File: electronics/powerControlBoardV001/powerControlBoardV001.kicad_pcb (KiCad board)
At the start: 2 copper layers, 100 x 100 mm, 45 parts, among them J1 Conn_01x03, J2 Conn_01x02, J3 Conn_01x02, K1 FINDER-40.52, Q1 Q_NMOS_GSD

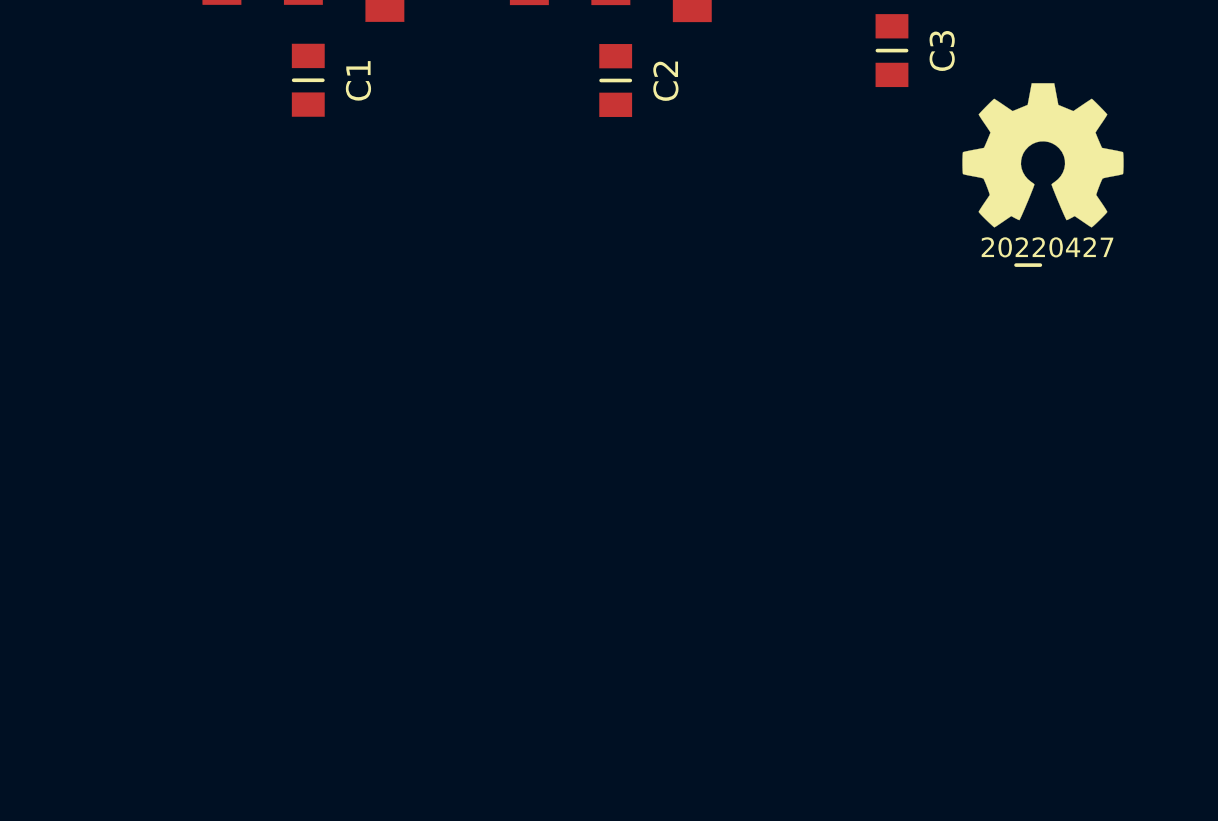
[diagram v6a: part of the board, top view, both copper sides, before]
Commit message: added full zerocross detector
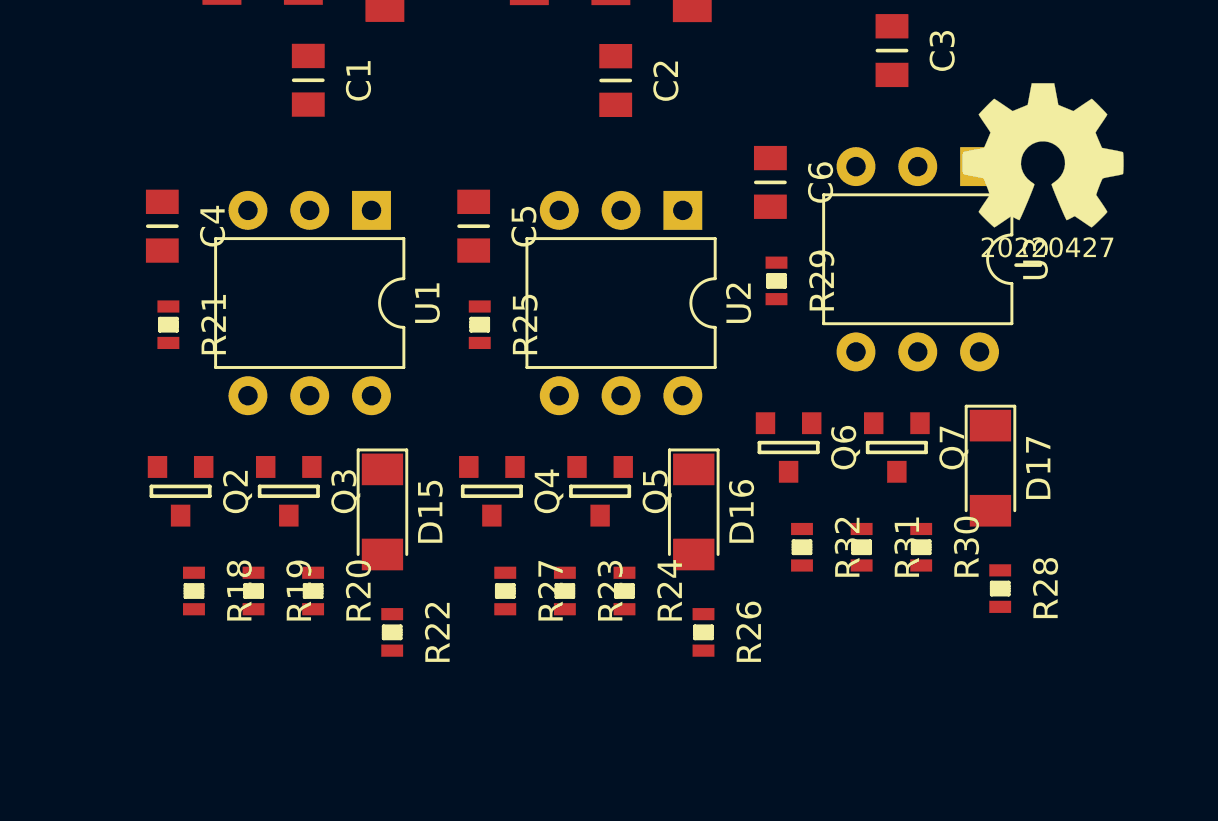
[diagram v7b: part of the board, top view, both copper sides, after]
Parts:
- added C4: 10u, SquantorRcl:C_0805, F.Cu at (102.5, 90.5)
- added C5: 10u, SquantorRcl:C_0805, F.Cu at (115.3, 90.5)
- added C6: 10u, SquantorRcl:C_0805, F.Cu at (127.5, 88.7)
- added D15: 1N4148, Diode_SMD:D_MiniMELF, F.Cu at (111.5, 102.2)
- added D16: 1N4148, Diode_SMD:D_MiniMELF, F.Cu at (124.3, 102.2)
- added D17: 1N4148, Diode_SMD:D_MiniMELF, F.Cu at (136.6, 100.5)
- added Q2: MMBT3904, SquantorIC:SOT23-3, F.Cu at (103.2, 101.4)
- added Q3: MMBT3904, SquantorIC:SOT23-3, F.Cu at (107.7, 101.4)
- added Q4: MMBT3904, SquantorIC:SOT23-3, F.Cu at (116.0, 101.4)
- added Q5: MMBT3904, SquantorIC:SOT23-3, F.Cu at (120.5, 101.4)
- added Q6: MMBT3904, SquantorIC:SOT23-3, F.Cu at (128.2, 99.6)
- added Q7: MMBT3904, SquantorIC:SOT23-3, F.Cu at (132.7, 99.6)
- added R18: 1K, SquantorRcl:R_0603, F.Cu at (103.8, 105.5)
- added R19: 2.2M, SquantorRcl:R_0603, F.Cu at (106.2, 105.5)
- added R20: 1K, SquantorRcl:R_0603, F.Cu at (108.7, 105.5)
- added R21: 47, SquantorRcl:R_0603, F.Cu at (102.8, 94.5)
- added R22: 1K, SquantorRcl:R_0603, F.Cu at (112.0, 107.2)
- added R23: 1K, SquantorRcl:R_0603, F.Cu at (119.0, 105.5)
- added R24: 2.2M, SquantorRcl:R_0603, F.Cu at (121.5, 105.5)
- added R25: 1K, SquantorRcl:R_0603, F.Cu at (115.5, 94.5)
- added R26: 47, SquantorRcl:R_0603, F.Cu at (124.8, 107.2)
- added R27: 1K, SquantorRcl:R_0603, F.Cu at (116.6, 105.5)
- added R28: 1K, SquantorRcl:R_0603, F.Cu at (136.9, 105.4)
- added R29: 2.2M, SquantorRcl:R_0603, F.Cu at (127.8, 92.8)
- added R30: 1K, SquantorRcl:R_0603, F.Cu at (133.7, 103.7)
- added R31: 47, SquantorRcl:R_0603, F.Cu at (131.2, 103.7)
- added R32: 1K, SquantorRcl:R_0603, F.Cu at (128.8, 103.7)
- added U1: 4N28, Package_DIP:DIP-6_W7.62mm, F.Cu at (111.1, 89.8)
- added U2: 4N28, Package_DIP:DIP-6_W7.62mm, F.Cu at (123.9, 89.8)
- added U3: 4N28, Package_DIP:DIP-6_W7.62mm, F.Cu at (136.1, 88.0)

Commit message: updated pcb to kicad 6 format
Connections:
- K1 pad 14: Net-(K1-Pad14) -> unconnected-(K1-Pad14)
- K1 pad 22: Net-(K1-Pad22) -> unconnected-(K1-Pad22)
- U1 pad 3: Net-(U1-Pad3) -> unconnected-(U1-Pad3)
- U2 pad 3: Net-(U2-Pad3) -> unconnected-(U2-Pad3)
- U3 pad 3: Net-(U3-Pad3) -> unconnected-(U3-Pad3)
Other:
- net class Default removed
